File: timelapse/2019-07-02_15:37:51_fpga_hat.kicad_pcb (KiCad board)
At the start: 4 copper layers, 65 x 56.5 mm, 90 parts, among them J1 2x20, J2 AudioJack3, J3 Conn_02x06_Top_Bottom, J4 Conn_02x06_Top_Bottom, J5 Conn_02x06_Top_Bottom, J6 Conn_01x02, SW1 PTS815, SW2 PTS815, SW3 PTS815, SW4 PTS815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

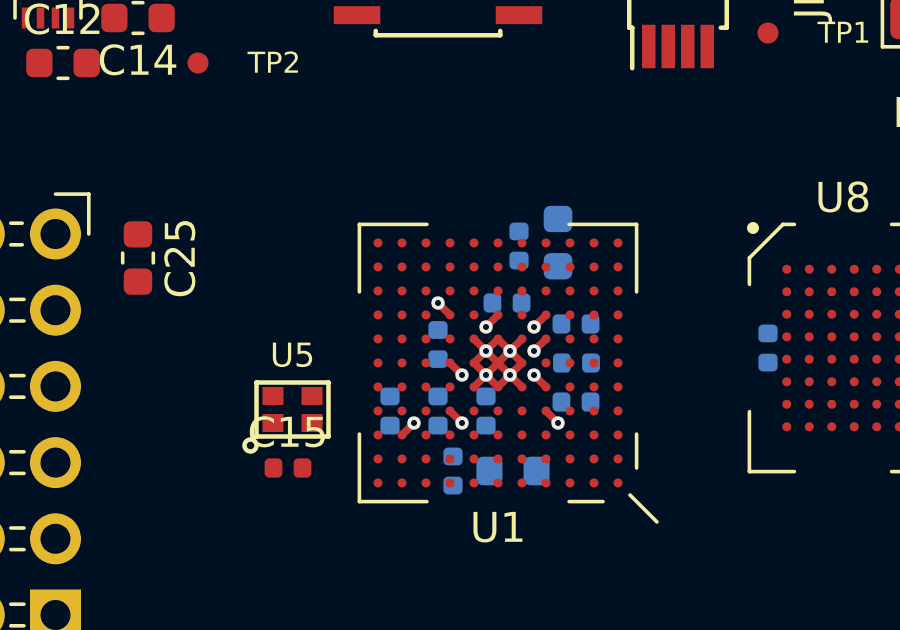
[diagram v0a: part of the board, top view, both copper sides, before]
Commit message: First run at power planes under FPGA
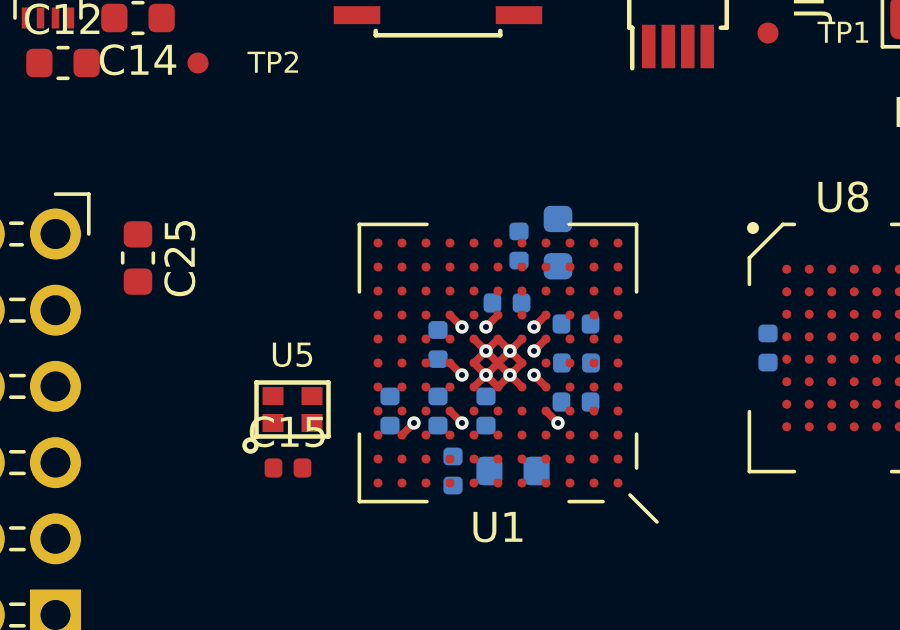
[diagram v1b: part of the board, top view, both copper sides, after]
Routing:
- removed copper zone on In2.Cu, net +1V2
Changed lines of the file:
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@@
     (solder_mask_min_width 0.1)
     (aux_axis_origin 0 0)
-    (visible_elements FFFFF77F)
+    (visible_elements FFFFFF7F)
     (pcbplotparams
       (layerselection 0x010fc_ffffffff)
@@
   (segment (start 132.9 106.1) (end 133.3 106.5) (width 0.25) (layer F.Cu) (net 1))
   (segment (start 132.1 106.1) (end 132.5 106.5) (width 0.25) (layer F.Cu) (net 1))
+  (via (at 131.3 105.3) (size 0.45) (drill 0.2) (layers F.Cu B.Cu) (net 2))
+  (segment (start 130.9 104.9) (end 131.3 105.3) (width 0.25) (layer F.Cu) (net 2))
   (via (at 133.7 105.3) (size 0.45) (drill 0.2) (layers F.Cu B.Cu) (net 2))
   (segment (start 134.1 104.9) (end 133.7 105.3) (width 0.25) (layer F.Cu) (net 2))
@@
   (segment (start 130.9 108.1) (end 131.3 108.5) (width 0.25) (layer F.Cu) (net 2))
   (via (at 131.3 108.5) (size 0.45) (drill 0.2) (layers F.Cu B.Cu) (net 2))
-  (via (at 130.5 104.5) (size 0.45) (drill 0.2) (layers F.Cu B.Cu) (net 2))
-  (segment (start 130.9 104.9) (end 130.5 104.5) (width 0.25) (layer F.Cu) (net 2))
   (via (at 131.3 106.9) (size 0.45) (drill 0.2) (layers F.Cu B.Cu) (net 7))
   (segment (start 130.9 106.5) (end 131.3 106.9) (width 0.25) (layer F.Cu) (net 7))
@@
     (connect_pads (clearance 0.2))
     (min_thickness 0.2)
-    (fill yes (arc_segments 32) (thermal_gap 0.21) (thermal_bridge_width 0.21))
+    (fill (arc_segments 32) (thermal_gap 0.21) (thermal_bridge_width 0.21))
     (polygon
       (pts
@@
     (connect_pads (clearance 0.2))
     (min_thickness 0.2)
-    (fill yes (arc_segments 32) (thermal_gap 0.21) (thermal_bridge_width 0.21))
+    (fill (arc_segments 32) (thermal_gap 0.21) (thermal_bridge_width 0.21))
     (polygon
       (pts
@@
       )
     )
-  )
-  (zone (net 2) (net_name +1V2) (layer In2.Cu) (hatch edge 0.508)
-    (priority 1)
-    (connect_pads (clearance 0.2))
-    (min_thickness 0.2)
-    (fill yes (arc_segments 32) (thermal_gap 0.21) (thermal_bridge_width 0.21))
-    (polygon
-      (pts
-        (xy 134.6 105.1) (xy 134.1 105.6) (xy 133.6 105.6) (xy 132.9 104.9) (xy 131.9 104.9)
-        (xy 131.2 104.9) (xy 130.9 105.2) (xy 130.9 105.5) (xy 130.9 106.1) (xy 130.9 107.4)
-        (xy 132.2 108.7) (xy 133.8 108.7) (xy 134.4 108.1) (xy 134.7 108.1) (xy 135.1 108.5)
-        (xy 135.1 109.2) (xy 134.7 109.6) (xy 131.6 109.6) (xy 129.7 107.7) (xy 119.9 97.9)
-        (xy 119.9 91.8) (xy 122.3 91.8) (xy 123.8 93.3) (xy 123.8 98.1) (xy 128.6 102.9)
-        (xy 134.6 102.9)
-      )
-    )
